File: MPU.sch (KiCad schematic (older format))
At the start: 28 parts, among them J2 Conn_02x10_Counter_Clockwise, J3 Micro_SD_Card, J4 USB_A, SW1 SW_DIP_x03, SW2 SW_Push, SW3 SW_Push, U1 STM32MP151AAB3, Y1 24MHz, Y2 32.768KHz

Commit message: Fix footprints
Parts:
- J4: footprint Connector_USB:USB_A_CNCTech_1001-011-01101_Horizontal -> Connector_USB:USB_A_Stewart_SS-52100-001_Horizontal
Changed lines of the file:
@@
 F 0 "J4" H 7607 6017 50  0000 C CNN
 F 1 "USB_A" H 7607 5926 50  0000 C CNN
-F 2 "Connector_USB:USB_A_CNCTech_1001-011-01101_Horizontal" H 7700 5500 50  0001 C CNN
+F 2 "Connector_USB:USB_A_Stewart_SS-52100-001_Horizontal" H 7700 5500 50  0001 C CNN
 F 3 " ~" H 7700 5500 50  0001 C CNN
 	1    7550 5550

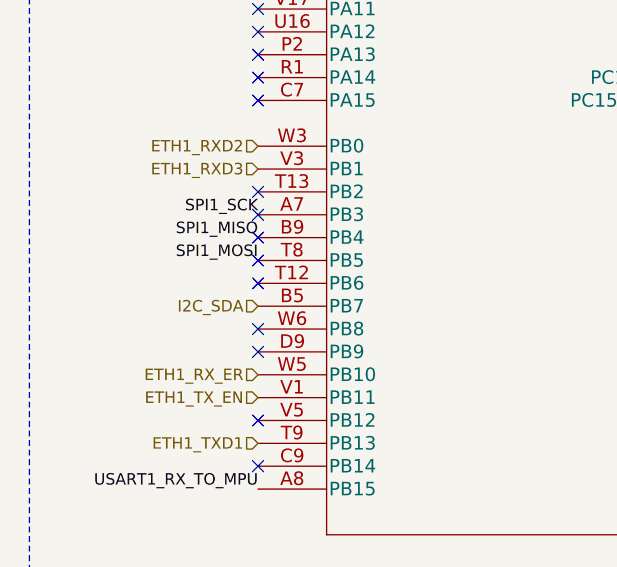
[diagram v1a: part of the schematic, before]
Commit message: Add mounting holes
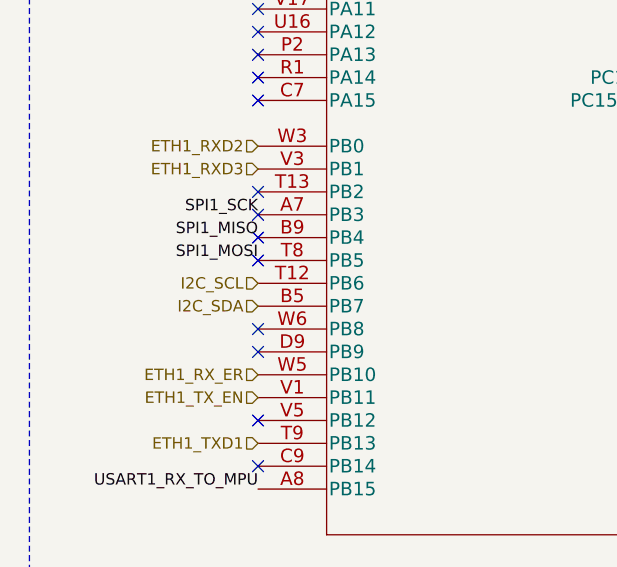
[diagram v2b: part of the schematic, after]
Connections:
- net I2C_SCL: now also U1.T12 (PB6)
- no-connect marks 45 -> 44
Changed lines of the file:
@@
 Text Label 4150 3950 0    50   ~ 0
 GPIO5
-NoConn ~ 1750 3350
 Text HLabel 3700 5850 0    50   Input ~ 0
 VDD
@@
 NoConn ~ 5500 2050
 NoConn ~ 5500 2150
+Text HLabel 1750 3350 0    50   Input ~ 0
+I2C_SCL
 $EndSCHEMATC
